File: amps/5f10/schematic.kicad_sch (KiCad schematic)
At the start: 42 parts, among them T1 PP OT

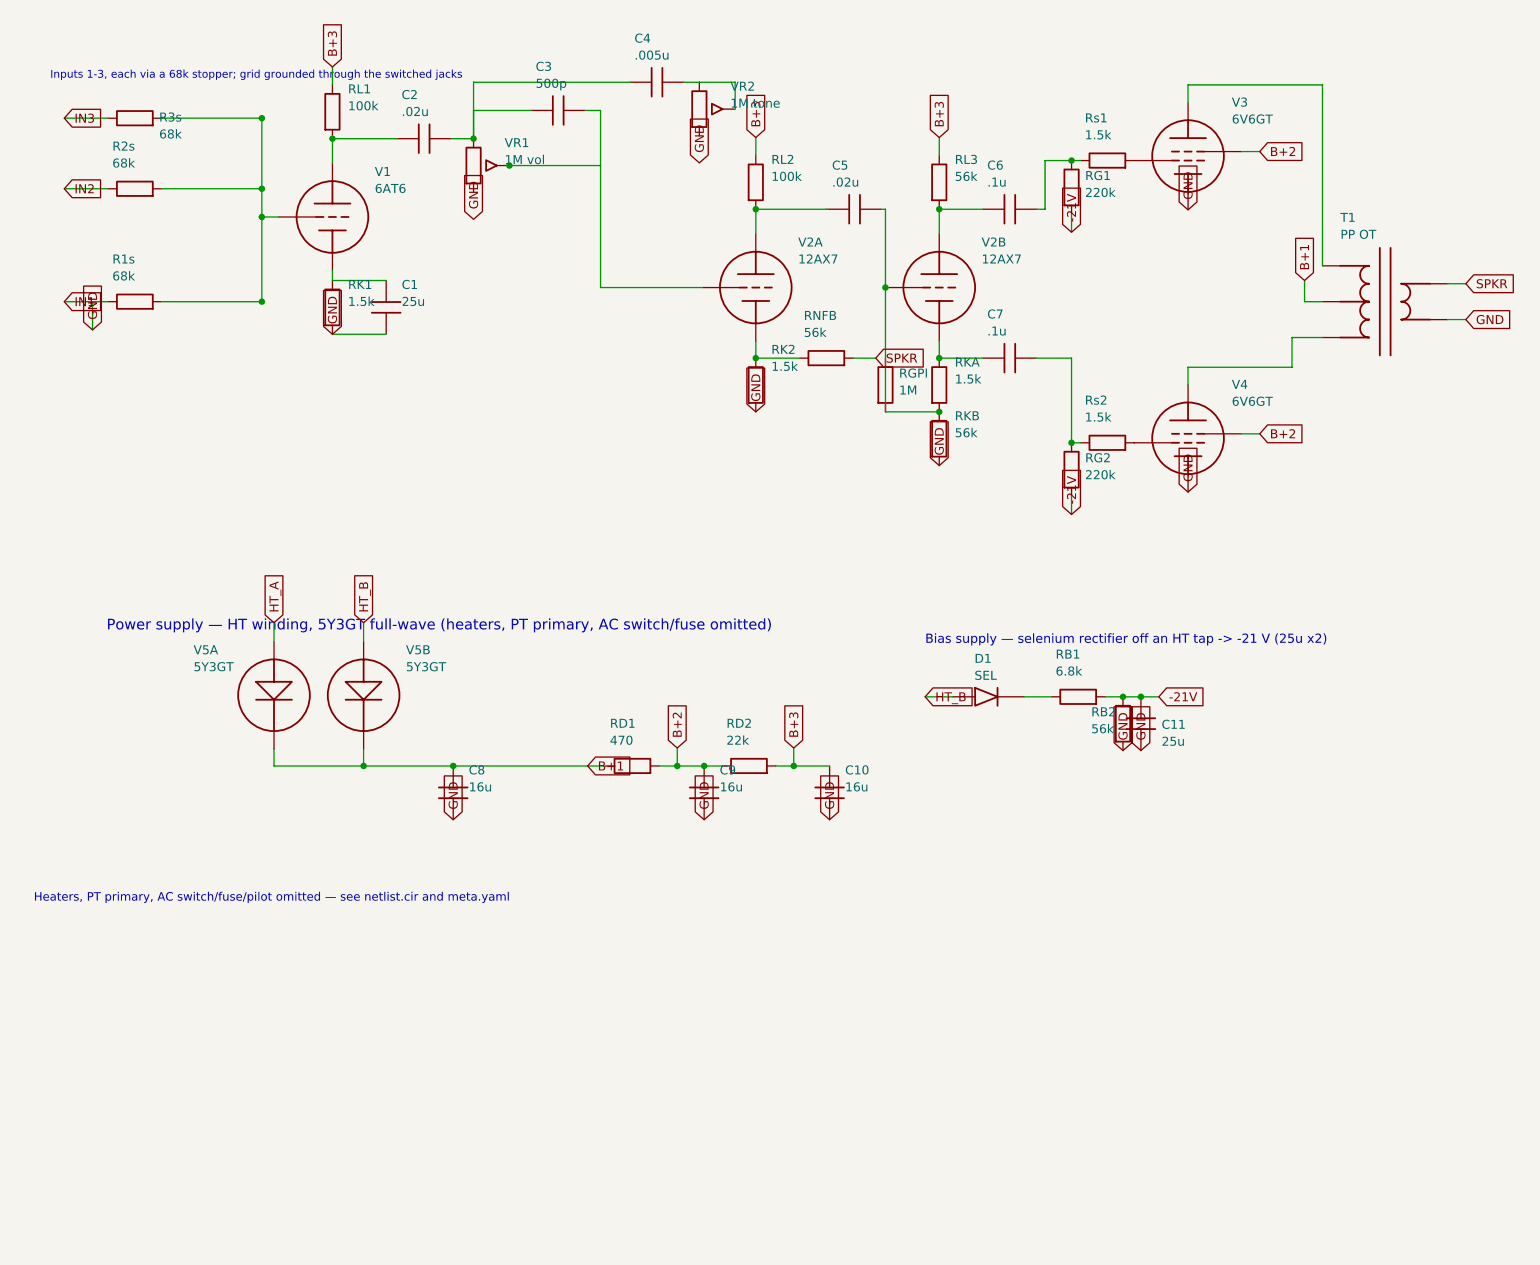
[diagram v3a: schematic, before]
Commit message: Fix: rotated global labels lettered their net names outside the flag
Every global label this pipeline emitted carried (justify left) regardless of
rotation. KiCanvas — like KiCad — draws label text horizontally at 0/180 and
vertically at 90/270 and reads WHICH SIDE of the anchor it letters on from the
justification, so at 180 and 270 the name printed outside an empty flag
outline, struck through by the very wire it names: 219 labels at 180 deg
(including the input-jack flags at top-left of nearly every sheet, the first
glyphs a visitor reads) and 792 GND/rail flags at 270 whose names squeezed at
the flag mouth instead of lettering down the body. The library already
compensated rotation for property text (`pa`); this mirrors that logic for
global labels: justify right at 180/270, left at 0/90.

check_schematics gains the geometry clause whose absence let all 1011
instances through a "no lettering through circuitry" pass: it modelled the
flag box but never the label TEXT, so a name rendered on the wrong side was
invisible to it. The gate now proves justification compensates rotation on
every global label.

Two more things this exposed, fixed in the same engine pass:

- Placement now measures with the renderer's own Newstroke advance table
  (extracted from the vendored kicanvas.js) instead of a flat 0.68-em prose
  average that under-read part lettering by a quarter — the mechanism behind
  every "metered clean, printed through its neighbour" incident. The GATE
  deliberately keeps the coarse ruler: re-ruling it with renderer truth was
  tried and red-flagged 28 of 34 sheets over abutments three visual passes
  had already judged sub-visual (the two-rulers note in schematic_lib.py).
- place_captions' escape ladder runs further, because a banner caption
  measured truly is half again wider than the old estimate believed.

All 34 schematics regenerated; full gate suite green.

🤖 Generated with [Claude Code](https://claude.com/claude-code)

Co-Authored-By: Claude Fable 5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
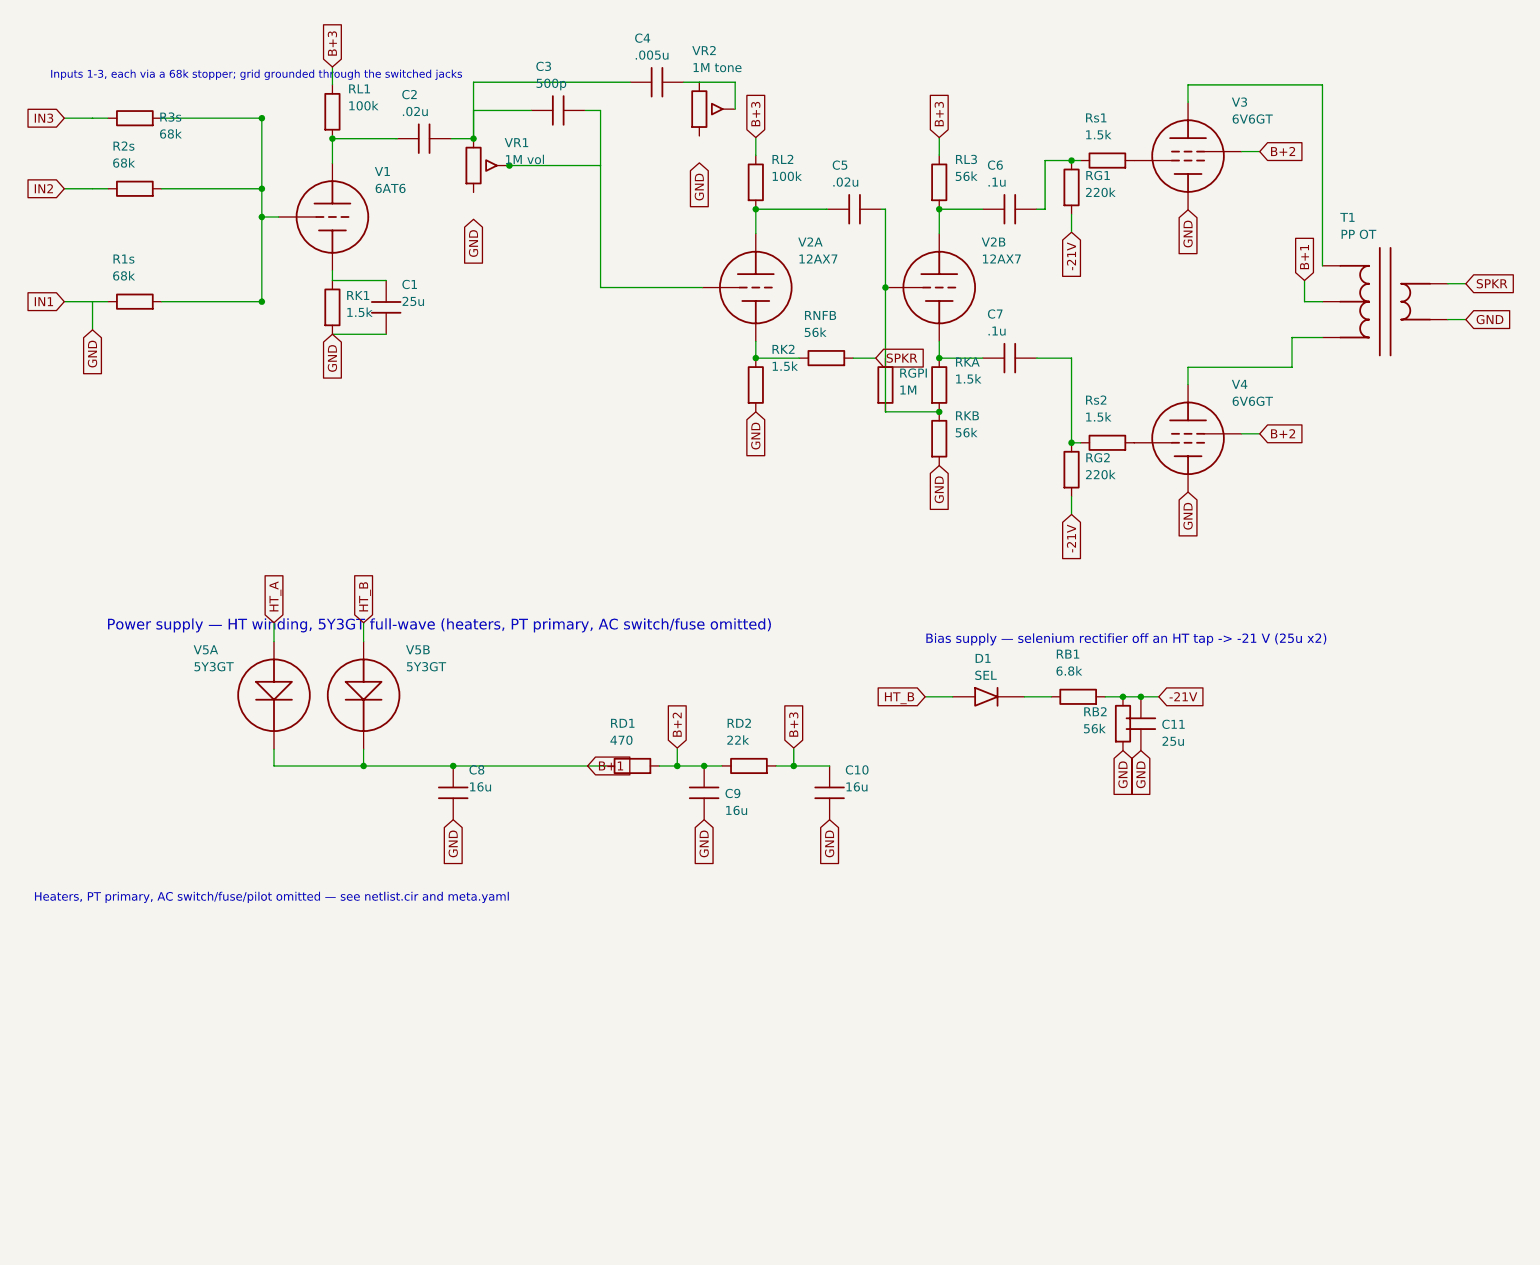
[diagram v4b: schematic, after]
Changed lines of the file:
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@@
     (comment 3 "Values read from: https://el34world.com/charts/Schematics/files/Fender/Fender_harvard_5f10_schem.pdf"))
   (global_label "IN3" (shape input) (at 17.018 24.889 180)
-    (effects (font (size 1.27 1.27)) (justify left)))
+    (effects (font (size 1.27 1.27)) (justify right)))
   (wire (pts (xy 17.018 24.889) (xy 21.018 24.889))
     (stroke (width 0) (type default)))
@@
   (junction (at 45.018 24.889) (diameter 0) (color 0 0 0 0))
   (global_label "IN2" (shape input) (at 17.018 34.889 180)
-    (effects (font (size 1.27 1.27)) (justify left)))
+    (effects (font (size 1.27 1.27)) (justify right)))
   (wire (pts (xy 17.018 34.889) (xy 21.018 34.889))
     (stroke (width 0) (type default)))
@@
   (junction (at 45.018 34.889) (diameter 0) (color 0 0 0 0))
   (global_label "IN1" (shape input) (at 17.018 50.889 180)
-    (effects (font (size 1.27 1.27)) (justify left)))
+    (effects (font (size 1.27 1.27)) (justify right)))
   (wire (pts (xy 17.018 50.889) (xy 21.018 50.889))
     (stroke (width 0) (type default)))
@@
   (junction (at 45.018 50.889) (diameter 0) (color 0 0 0 0))
   (global_label "GND" (shape input) (at 21.018 54.889 270)
-    (effects (font (size 1.27 1.27)) (justify left)))
+    (effects (font (size 1.27 1.27)) (justify right)))
   (wire (pts (xy 21.018 50.889) (xy 21.018 54.889))
     (stroke (width 0) (type default)))
@@
   (symbol (lib_id "cx:R") (at 55.018 51.699 0) (unit 1)
     (in_bom yes) (on_board yes)
-    (property "Reference" "RK1" (at 57.218 48.499 0) (effects (font (size 1.27 1.27)) (justify left)))
-    (property "Value" "1.5k" (at 57.218 50.899 0) (effects (font (size 1.27 1.27)) (justify left))))
+    (property "Reference" "RK1" (at 56.934 50.059 0) (effects (font (size 1.27 1.27)) (justify left)))
+    (property "Value" "1.5k" (at 56.934 52.459 0) (effects (font (size 1.27 1.27)) (justify left))))
   (symbol (lib_id "cx:C") (at 62.638 51.699 0) (unit 1)
     (in_bom yes) (on_board yes)
@@
     (stroke (width 0) (type default)))
   (global_label "GND" (shape input) (at 55.018 55.509 270)
-    (effects (font (size 1.27 1.27)) (justify left)))
+    (effects (font (size 1.27 1.27)) (justify right)))
   (wire (pts (xy 55.018 27.789) (xy 64.018 27.789))
     (stroke (width 0) (type default)))
@@
     (property "Value" "1M vol" (at 79.418 30.799 0) (effects (font (size 1.27 1.27)) (justify left))))
   (global_label "GND" (shape input) (at 75.018 39.219 270)
-    (effects (font (size 1.27 1.27)) (justify left)))
+    (effects (font (size 1.27 1.27)) (justify right)))
   (wire (pts (xy 75.018 27.789) (xy 75.018 23.789))
     (stroke (width 0) (type default)))
@@
   (symbol (lib_id "cx:POT") (at 107.018 23.599 0) (unit 1)
     (in_bom yes) (on_board yes)
-    (property "Reference" "VR2" (at 111.418 20.399 0) (effects (font (size 1.27 1.27)) (justify left)))
-    (property "Value" "1M tone" (at 111.418 22.799 0) (effects (font (size 1.27 1.27)) (justify left))))
+    (property "Reference" "VR2" (at 106.002 15.359 0) (effects (font (size 1.27 1.27)) (justify left)))
+    (property "Value" "1M tone" (at 106.002 17.759 0) (effects (font (size 1.27 1.27)) (justify left))))
   (global_label "GND" (shape input) (at 107.018 31.219 270)
-    (effects (font (size 1.27 1.27)) (justify left)))
+    (effects (font (size 1.27 1.27)) (justify right)))
   (wire (pts (xy 112.098 23.599) (xy 112.098 19.789))
     (stroke (width 0) (type default)))
@@
     (property "Value" "1.5k" (at 117.218 60.099 0) (effects (font (size 1.27 1.27)) (justify left))))
   (global_label "GND" (shape input) (at 115.018 66.509 270)
-    (effects (font (size 1.27 1.27)) (justify left)))
+    (effects (font (size 1.27 1.27)) (justify right)))
   (symbol (lib_id "cx:R") (at 125.018 58.889 90) (unit 1)
     (in_bom yes) (on_board yes)
@@
     (property "Value" "56k" (at 143.218 69.509 0) (effects (font (size 1.27 1.27)) (justify left))))
   (global_label "GND" (shape input) (at 141.018 74.119 270)
-    (effects (font (size 1.27 1.27)) (justify left)))
+    (effects (font (size 1.27 1.27)) (justify right)))
   (wire (pts (xy 133.398 48.889) (xy 133.398 66.509))
     (stroke (width 0) (type default)))
@@
     (stroke (width 0) (type default)))
   (global_label "-21V" (shape input) (at 159.768 41.049 270)
-    (effects (font (size 1.27 1.27)) (justify left)))
+    (effects (font (size 1.27 1.27)) (justify right)))
   (wire (pts (xy 183.898 29.619) (xy 186.438 29.619))
     (stroke (width 0) (type default)))
@@
     (effects (font (size 1.27 1.27)) (justify left)))
   (global_label "GND" (shape input) (at 176.278 37.874 270)
-    (effects (font (size 1.27 1.27)) (justify left)))
+    (effects (font (size 1.27 1.27)) (justify right)))
   (symbol (lib_id "cx:R") (at 164.848 70.889 90) (unit 1)
     (in_bom yes) (on_board yes)
@@
     (stroke (width 0) (type default)))
   (global_label "-21V" (shape input) (at 159.768 81.049 270)
-    (effects (font (size 1.27 1.27)) (justify left)))
+    (effects (font (size 1.27 1.27)) (justify right)))
   (wire (pts (xy 183.898 69.619) (xy 186.438 69.619))
     (stroke (width 0) (type default)))
@@
     (effects (font (size 1.27 1.27)) (justify left)))
   (global_label "GND" (shape input) (at 176.278 77.874 270)
-    (effects (font (size 1.27 1.27)) (justify left)))
+    (effects (font (size 1.27 1.27)) (justify right)))
   (symbol (lib_id "cx:OT_PP") (at 204.218 50.889 0) (unit 1)
     (in_bom yes) (on_board yes)
@@
     (property "Value" "16u" (at 74.338 119.699 0) (effects (font (size 1.27 1.27)) (justify left))))
   (global_label "GND" (shape input) (at 72.138 124.309 270)
-    (effects (font (size 1.27 1.27)) (justify left)))
+    (effects (font (size 1.27 1.27)) (justify right)))
   (global_label "B+1" (shape input) (at 91.188 116.689 0)
     (effects (font (size 1.27 1.27)) (justify left)))
@@
   (symbol (lib_id "cx:C") (at 107.698 120.499 0) (unit 1)
     (in_bom yes) (on_board yes)
-    (property "Reference" "C9" (at 109.898 117.299 0) (effects (font (size 1.27 1.27)) (justify left)))
-    (property "Value" "16u" (at 109.898 119.699 0) (effects (font (size 1.27 1.27)) (justify left))))
+    (property "Reference" "C9" (at 110.63 120.637 0) (effects (font (size 1.27 1.27)) (justify left)))
+    (property "Value" "16u" (at 110.63 123.037 0) (effects (font (size 1.27 1.27)) (justify left))))
   (global_label "GND" (shape input) (at 107.698 124.309 270)
-    (effects (font (size 1.27 1.27)) (justify left)))
+    (effects (font (size 1.27 1.27)) (justify right)))
   (symbol (lib_id "cx:R") (at 114.048 116.689 90) (unit 1)
     (in_bom yes) (on_board yes)
@@
     (property "Value" "16u" (at 127.678 119.699 0) (effects (font (size 1.27 1.27)) (justify left))))
   (global_label "GND" (shape input) (at 125.478 124.309 270)
-    (effects (font (size 1.27 1.27)) (justify left)))
+    (effects (font (size 1.27 1.27)) (justify right)))
   (text "Bias supply — selenium rectifier off an HT tap -> -21 V (25u x2)" (at 139.018 98.889 0)
     (effects (font (size 1.3 1.3)) (justify left)))
   (global_label "HT_B" (shape input) (at 139.018 106.889 180)
-    (effects (font (size 1.27 1.27)) (justify left)))
+    (effects (font (size 1.27 1.27)) (justify right)))
   (wire (pts (xy 139.018 106.889) (xy 142.928 106.889))
     (stroke (width 0) (type default)))
@@
   (symbol (lib_id "cx:R") (at 167.058 110.699 0) (unit 1)
     (in_bom yes) (on_board yes)
-    (property "Reference" "RB2" (at 162.551 109.059 0) (effects (font (size 1.27 1.27)) (justify left)))
-    (property "Value" "56k" (at 162.551 111.459 0) (effects (font (size 1.27 1.27)) (justify left))))
+    (property "Reference" "RB2" (at 161.393 109.059 0) (effects (font (size 1.27 1.27)) (justify left)))
+    (property "Value" "56k" (at 161.393 111.459 0) (effects (font (size 1.27 1.27)) (justify left))))
   (global_label "GND" (shape input) (at 167.058 114.509 270)
-    (effects (font (size 1.27 1.27)) (justify left)))
+    (effects (font (size 1.27 1.27)) (justify right)))
   (junction (at 169.598 106.889) (diameter 0) (color 0 0 0 0))
   (symbol (lib_id "cx:C") (at 169.598 110.699 0) (unit 1)
@@
     (property "Value" "25u" (at 172.53 113.237 0) (effects (font (size 1.27 1.27)) (justify left))))
   (global_label "GND" (shape input) (at 169.598 114.509 270)
-    (effects (font (size 1.27 1.27)) (justify left)))
+    (effects (font (size 1.27 1.27)) (justify right)))
   (global_label "-21V" (shape input) (at 172.138 106.889 0)
     (effects (font (size 1.27 1.27)) (justify left)))
